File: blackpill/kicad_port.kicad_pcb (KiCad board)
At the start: 2 copper layers, 100 x 86 mm, 19 parts, among them J1 Conn_01x13, J2 Conn_01x13, J3 Conn_01x13, J4 Conn_01x13, J5 Conn_01x10, J6 Conn_01x10, M1 MountingHole_6.4mm_M6, M3 MountingHole_4.3mm_M4, M4 MountingHole_4.3mm_M4, U1 YAAJ_WeAct_BlackPill_Part_Lik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

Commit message: Add Advantage compatibility
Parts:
- added D5: D_Small, cftkb:D_DO-35_SOD27_P5.08mm_Horizontal, F.Cu at (161.9, 63.6)
- added SW1: RotaryEncoder_Switch, Keebio-Parts:RotaryEncoder_EC11, F.Cu at (150.0, 60.0)
- moved U1 4.79 mm to (165.8, 98.4)
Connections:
- U1 pad 42: unconnected-(U1-Pad42) -> /ENB
- U1 pad 43: unconnected-(U1-Pad43) -> /ENA
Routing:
- net /ENA: track 0.00 -> 51.1 mm, vias 0 -> 1
- net /ROW_0: track 29.6 -> 78.5 mm
- net /ENB: track 0.00 -> 48.1 mm, vias 0 -> 1
- net /COL_4: track 193.5 -> 227.6 mm
- net /COL_0: track 190.1 -> 176.9 mm
- net /ROW_4: track 86.8 -> 75.5 mm, vias 2 -> 1
- net /COL_5: track 235.4 -> 245.0 mm
- net Net-(SW1-PadS1): track 0.00 -> 7.30 mm
- net /ROW_9: track 58.7 -> 65.9 mm
- net /COL_2: track 195.5 -> 189.7 mm, vias 1 -> 0
- net /ROW_2: track 67.3 -> 61.5 mm, vias 0 -> 1
- net /COL_3: track 198.4 -> 203.2 mm, vias 2 -> 1
- net /ROW_F1: track 157.3 -> 162.1 mm
- net /COL_6: track 161.4 -> 166.2 mm
- net /3V3: track 75.2 -> 79.9 mm
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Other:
- board text added: "Kinesis Contoured/Advantage Blackpill + QMK Mod Fork of gitlab.com/Silman/kinesismod by dcpedit (Rev 2)"
- board text removed: "Kinesis Contoured/Advantage Blackpill + QMK Mod Fork of gitlab.com/Silman/kinesismod by dcpedit"

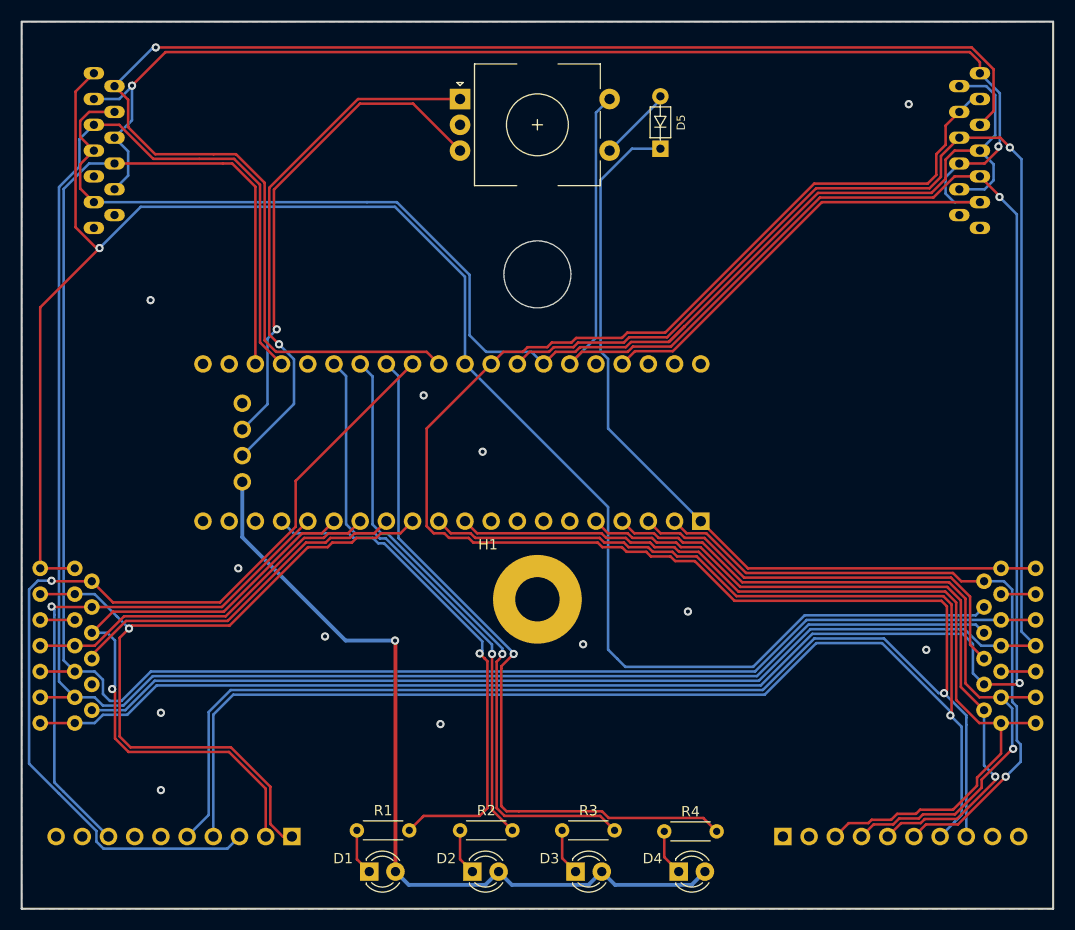
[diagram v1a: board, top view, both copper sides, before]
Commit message: Update readme with wireless info
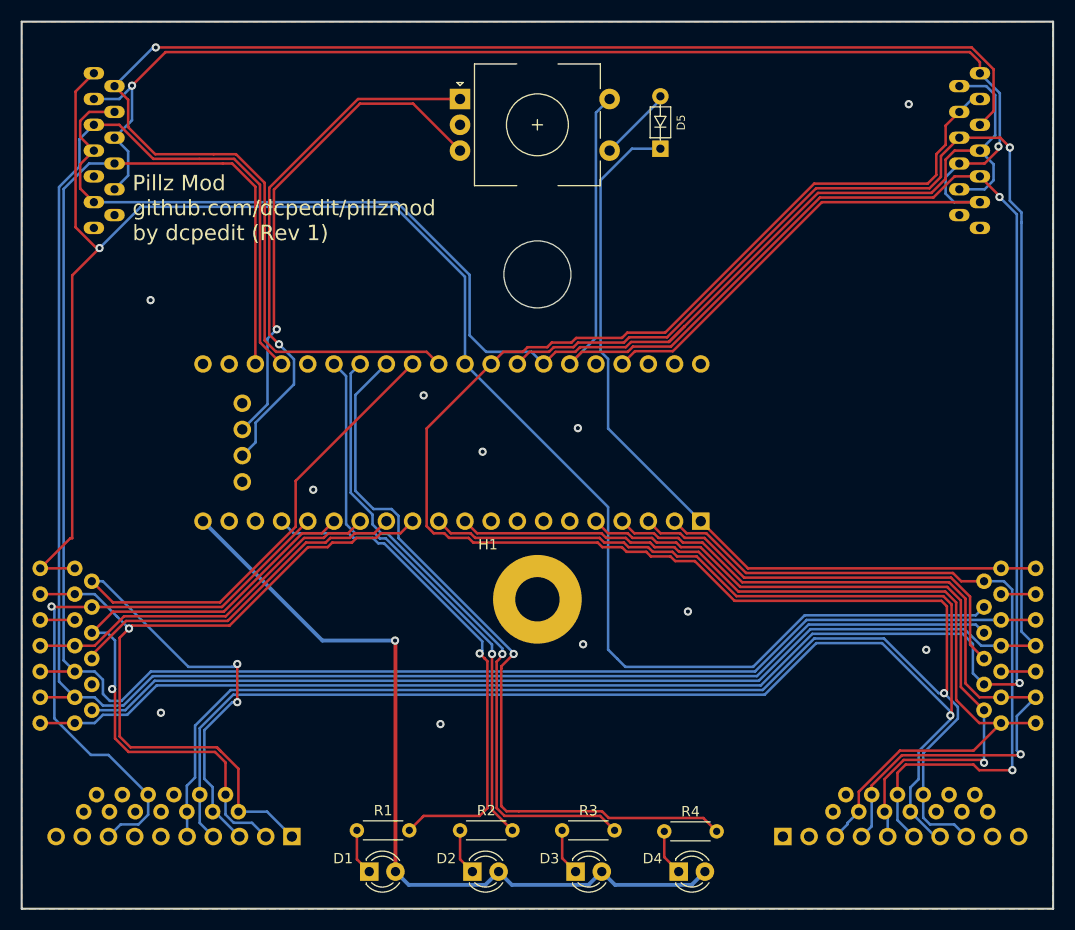
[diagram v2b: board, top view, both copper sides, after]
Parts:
- added J7: Conn_01x13, kinx:39-53-2135, B.Cu at (186.2, 126.6)
- added J8: Conn_01x13, kinx:39-53-2135, B.Cu at (113.5, 126.6)
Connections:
- U1 pad 20: unconnected-(U1-Pad20) -> /3V3
- U1 pad 44: /3V3 -> unconnected-(U1-3V3-Pad44)
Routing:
- net /ROW_5: track 92.4 -> 81.6 mm, vias 1 -> 2
- net /ROW_9: track 65.9 -> 71.5 mm
- net /ROW_3: track 52.9 -> 58.1 mm
- net /COL_5: track 245.0 -> 249.1 mm
- net /LED_KEYPAD: track 70.4 -> 73.9 mm
- net /ROW_7: track 76.1 -> 79.5 mm
- net /COL_6: track 166.2 -> 169.1 mm
- net /ROW_8: track 70.1 -> 71.4 mm
- net /ROW_6: track 91.8 -> 90.8 mm
- net /3V3: track 79.9 -> 79.0 mm
- net /ROW_4: track 75.5 -> 76.3 mm
- net /LED_SCROLL_LOCK: track 61.2 -> 61.9 mm
- net GND: vias 12 -> 11
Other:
- board text added: "KB600"
- board text added: "Molex 39-53-2135"
- board text added: "Pillz Mod github.com/dcpedit/pillzmod by dcpedit (Rev 1)"
- board text removed: "Kinesis Contoured/Advantage Blackpill + QMK Mod Fork of gitlab.com/Silman/kinesismod by dcpedit (Rev 2)"
